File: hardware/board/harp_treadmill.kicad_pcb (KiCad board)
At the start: 4 copper layers, 80 x 100 mm, 133 parts, among them J1 Conn_01x03_Male, J2 AudioJack3, J5 USB_C_Receptacle_USB2.0, J6 Barrel_Jack_Switch, Q1 IRF8707TRPBF, U1 LP2985-3.3, U10 AD8615, U11 INA180A4, U12 UCC27537, U13 LM27762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

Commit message: update sch and pcb
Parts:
- removed R42: 68, Resistor_SMD:R_0402_1005Metric
- removed R44: 49.9, Resistor_SMD:R_0402_1005Metric
- added C34: 100nF, Capacitor_SMD:C_0402_1005Metric, F.Cu at (112.9, 71.0)
- added C35: 100nF, Capacitor_SMD:C_0402_1005Metric, F.Cu at (118.1, 70.0)
- added C36: 100nF, Capacitor_SMD:C_0402_1005Metric, F.Cu at (112.4, 69.2)
- added C61: 1uF, Capacitor_SMD:C_0402_1005Metric, F.Cu at (111.9, 71.0)
- added C62: 10uF, Capacitor_SMD:C_0805_2012Metric, F.Cu at (103.3, 101.5)
- added H1: MountingHole_Pad, kicad_component_library:Terminal_Keystone_779x_EdgeMount_Horizontal, F.Cu at (107.6, 118.4)
- added J3: Conn_01x05_Female, Connector_Phoenix_MC:PhoenixContact_MC_1,5_5-G-3.5_1x05_P3.50mm_Horizontal, F.Cu at (108.1, 41.0)
- added J4: Conn_01x02_Female, Connector_Phoenix_MC:PhoenixContact_MC_1,5_2-G-3.5_1x02_P3.50mm_Horizontal, F.Cu at (108.1, 106.4)
- added J7: Conn_01x04_Female, Connector_Phoenix_MC:PhoenixContact_MC_1,5_4-G-3.5_1x04_P3.50mm_Horizontal, F.Cu at (108.1, 74.8)
- added R14: 10K, Resistor_SMD:R_0402_1005Metric, F.Cu at (111.4, 48.7)
- added R8: 10K, Resistor_SMD:R_0402_1005Metric, F.Cu at (111.4, 43.7)
- moved C41 148.2 mm to (142.4, 122.6), turned to 180 degrees
- moved C46 131.9 mm to (155.2, 94.0), turned to 90 degrees
- moved C49 128.7 mm to (155.2, 92.0), turned to 90 degrees
- moved C42 121.2 mm to (143.1, 116.0), turned to -90 degrees
- moved C43 117.8 mm to (144.4, 116.0), turned to -90 degrees
- moved C48 114.2 mm to (145.7, 116.0), turned to 90 degrees
- moved C8 107.9 mm to (170.5, 51.2), turned to 180 degrees
- moved C60 106.9 mm to (142.3, 46.8), turned to -90 degrees
- moved R31 106.7 mm to (147.2, 113.8), turned to 180 degrees
- moved C44 106.1 mm to (140.0, 44.4)
- moved R32 103.7 mm to (147.2, 114.8)
- moved C40 102.8 mm to (139.9, 42.9), turned to 180 degrees
- moved R22 102.6 mm to (144.4, 84.5), turned to 90 degrees
- moved R23 101.5 mm to (142.9, 84.5), turned to 90 degrees
- moved C39 100.7 mm to (133.1, 115.3)
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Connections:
- U15 pad 2: /Encoder/ENC_A -> /Encoder/ENC_B
- U15 pad 3: /Encoder/ENC_B -> /Encoder/ENC_A
- U4 pad 11: /Harp Core RP2040 + Isolated USB/PIO_POCI0 -> unconnected-(U4-GPIO8-Pad11)
- U4 pad 12: /Harp Core RP2040 + Isolated USB/PIO_SCK0 -> /Harp Core RP2040 + Isolated USB/PIO_CS0
- U4 pad 13: unconnected-(U4-GPIO10-Pad13) -> /Harp Core RP2040 + Isolated USB/PIO_POCI0
- U4 pad 14: /Harp Core RP2040 + Isolated USB/BRAKE_PWM -> /Harp Core RP2040 + Isolated USB/PIO_SCK0
- U4 pad 16: unconnected-(U4-GPIO13-Pad16) -> /Harp Core RP2040 + Isolated USB/BRAKE_PWM
- U4 pad 17: /Encoder/ENC_A -> unconnected-(U4-GPIO14-Pad17)
- U4 pad 18: /Encoder/ENC_B -> unconnected-(U4-GPIO15-Pad18)
- U4 pad 27: unconnected-(U4-GPIO16-Pad27) -> /Encoder/ENC_A
- U4 pad 28: unconnected-(U4-GPIO17-Pad28) -> /Encoder/ENC_B
- U4 pad 9: /Harp Core RP2040 + Isolated USB/PIO_CS0 -> unconnected-(U4-GPIO7-Pad9)
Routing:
- net /Harp Core RP2040 + Isolated USB/HARP_CLK_SYNC: track 6.47 -> 43.6 mm, vias 1 -> 0
- net /Harp Core RP2040 + Isolated USB/BRAKE_PWM: track 0.00 -> 36.2 mm
- net GND: track 31.6 -> 66.9 mm, vias 23 -> 47
- net Net-(U8-~{CS}): track 0.00 -> 33.9 mm
- net /Harp Core RP2040 + Isolated USB/PIO_POCI0: track 0.00 -> 32.9 mm
- net Net-(U8-SCLK): track 0.00 -> 31.3 mm
- net Net-(U9-SCLK): track 0.00 -> 28.5 mm
- net /Harp Core RP2040 + Isolated USB/PIO_POCI1: track 0.00 -> 27.4 mm
- net Net-(U9-~{CS}): track 0.00 -> 26.2 mm
- net Net-(J7-Pin_3): track 0.00 -> 23.6 mm, vias 0 -> 1
- net Net-(J7-Pin_2): track 0.00 -> 23.5 mm, vias 0 -> 1
- net VIN1: track 0.00 -> 17.6 mm, vias 0 -> 5
- net (no net): track 17.3 -> 0.00 mm, vias 6 -> 0
- net GND2: track 0.00 -> 16.7 mm
- net VREF_1V65: track 0.00 -> 15.9 mm, vias 0 -> 3
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- added copper zone on In2.Cu, net +12V
- added copper zone on In2.Cu, net +3V3
- added copper zone on In2.Cu, net +5V
- added copper zone on In2.Cu, net -5V
- added copper zone on In2.Cu, net 5V2
- added copper zone on In2.Cu, net VREF_1V65
- added copper zone on In2.Cu, net VREF_3V3
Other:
- board text added: "5V →"
- board text added: "A →"
- board text added: "B →"
- board text added: "Black →"
- board text added: "DC Power 13-25V"
- board text added: "Fits in: Hammond Manufacturing 1455L801"
- board text added: "GND →"
- board text added: "Green →"
- board text added: "Harp Sync Input ↓"
- board text added: "Red →"
- board text added: "Shield →"
- board text added: "TODO: RFID TODO: OSH Logo"
- board text added: "TODO: Switch 5v2 and 12v"
- board text added: "TODO: remove slot in USBC footprint. TODO: capacitors on 12V source?"
- board text added: "White →"
- board text removed: "Harp Sync Input ↑"
- board text removed: "Power"
- board text removed: "TODO: add a GND LUG?"
- board text removed: "TODO: remove slot in USBC footprint."

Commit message: update schematic; continue pcb draft
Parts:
- removed R14, R8: 10K, Resistor_SMD:R_0402_1005Metric
- added C20: 100pF, Capacitor_SMD:C_0402_1005Metric, F.Cu at (112.5, 44.1)
- added C21: 1000pF, Capacitor_SMD:C_0402_1005Metric, F.Cu at (113.6, 46.2)
- added C22: 100pF, Capacitor_SMD:C_0402_1005Metric, F.Cu at (112.5, 48.3)
- added C23: 100nF, Capacitor_SMD:C_0402_1005Metric, F.Cu at (119.9, 43.2)
- added C25: 100nF, Capacitor_SMD:C_0402_1005Metric, F.Cu at (119.8, 49.2)
- added G***: LOGO, LOGO, B.Cu at (169.5, 100.0)
- added REF**: OSHW-Logo2_7.3x6mm_SilkScreen, Symbol:OSHW-Logo2_7.3x6mm_SilkScreen, B.Cu at (170.6, 126.0)
- added REF**: Symbol_Barrel_Polarity, Symbol:Symbol_Barrel_Polarity, B.Cu at (170.2, 118.0)
- added RN1: 20K, Resistor_SMD:R_Array_Convex_2x0606, F.Cu at (111.8, 46.2)
- R15: footprint Resistor_SMD:R_0603_1608Metric -> Resistor_SMD:R_0603_1608Metric_Pad0.98x0.95mm_HandSolder
- R29: value 1K82 -> 715
- R32: value 715 -> 1K82
- moved R16 12.9 mm to (114.2, 53.4)
- moved C27 12.2 mm to (115.3, 53.4), turned to 90 degrees
- moved R17 12.2 mm to (115.9, 51.9), turned to 180 degrees
- moved C45 6.48 mm to (154.9, 96.4), turned to 0 degrees
- moved C62 5.25 mm to (108.5, 102.2), turned to 180 degrees
- moved R27 5.12 mm to (111.6, 103.6), turned to -90 degrees
- moved C59 4.74 mm to (117.2, 104.3)
- moved U11 4.70 mm to (114.5, 103.7)
- moved C30 4.50 mm to (112.1, 98.9)
- moved U10 4.49 mm to (114.5, 98.9)
- moved TP1 3.99 mm to (127.0, 43.6), turned to 0 degrees
- moved C11 3.34 mm to (152.5, 93.5), turned to -90 degrees
- moved C46 3.29 mm to (156.3, 90.9), turned to 180 degrees
- moved TP2 3.11 mm to (111.4, 94.5), turned to 180 degrees
- moved D5 2.80 mm to (126.5, 45.6)
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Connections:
- C24 pad 1: GND -> +5V
- C24 pad 2: +5V -> GND
- C39 pad 1: 5V2 -> +12V
- C52 pad 1: +12V -> 5V2
- C55 pad 1: +5V -> 5V2
- C57 pad 1: +5V -> 5V2
- C58 pad 2: +5V -> 5V2
- D9 pad 1: Net-(U14-BOOST2) -> Net-(U14-BOOST1)
- D9 pad 2: Net-(U14-BOOST1) -> Net-(U14-BOOST2)
- J7 pad 1: +5V -> 5V2
- L2 pad 1: 5V2 -> +12V
- L3 pad 2: +12V -> 5V2
- R28 pad 2: 5V2 -> +12V
- R29 pad 1: GND -> Net-(U14-FB1)
- R29 pad 2: Net-(U14-FB1) -> GND
- R32 pad 1: Net-(U14-FB2) -> GND
- R32 pad 2: GND -> Net-(U14-FB2)
- R35 pad 1: +12V -> 5V2
- U15 pad 8: +5V -> 5V2
- U4 pad 16: /Harp Core RP2040 + Isolated USB/BRAKE_PWM -> unconnected-(U4-GPIO13-Pad16)
- U4 pad 35: unconnected-(U4-GPIO23-Pad35) -> /Harp Core RP2040 + Isolated USB/BRAKE_PWM
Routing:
- net 5V2: track 6.57 -> 62.1 mm, vias 1 -> 15
- net +3V3: track 43.8 -> 91.5 mm, vias 19 -> 27
- net GND: track 66.9 -> 97.8 mm, vias 47 -> 88
- net -5V: track 1.15 -> 12.2 mm, vias 1 -> 5
- net Net-(D5-K): track 9.06 -> 18.5 mm
- net Net-(D8-K): track 0.00 -> 8.85 mm
- net Net-(D10-K): track 0.00 -> 8.85 mm
- net +12V: track 14.6 -> 22.8 mm, vias 4 -> 8
- net +5V: track 7.44 -> 13.6 mm, vias 1 -> 4
- net Net-(U14-BOOST1): track 0.00 -> 5.96 mm, vias 0 -> 2
- net Net-(U14-BOOST2): track 0.00 -> 5.91 mm, vias 0 -> 2
- net Net-(U10--): track 6.34 -> 10.4 mm
- net Net-(RN1A-R1.2): track 3.13 -> 7.04 mm
- net VREF_1V65: track 15.9 -> 19.7 mm
- net Net-(RN1B-R2.2): track 3.31 -> 7.04 mm
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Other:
- board text added: "+"
- board text added: "-"
- board text added: "DC Power 13-25V, 6W"
- board text added: "Ground"
- board text added: "Oct 31, 2023"
- board text added: "Shield → (if provided)"
- board text added: "Source Files & Setup ↓"
- board text added: "TODO: remove slot in USBC footprint."
- board text removed: "DC Power 13-25V"
- board text removed: "Oct 26, 2023"
- board text removed: "Shield →"
- board text removed: "TODO: RFID TODO: OSH Logo"
- board text removed: "TODO: Switch 5v2 and 12v"
- board text removed: "TODO: remove slot in USBC footprint. TODO: capacitors on 12V source?"

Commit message: wrap up pcb draft
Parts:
- removed D5: D_Zener, Diode_SMD:D_SOD-123F
- added C63: 100nF, Capacitor_SMD:C_0402_1005Metric, F.Cu at (115.7, 53.3)
- added R8: 10K, Resistor_SMD:R_0402_1005Metric, F.Cu at (118.2, 48.9)
- added U16: AD8615, Package_TO_SOT_SMD:TSOT-23-5, F.Cu at (115.6, 51.0)
- moved TP1 20.9 mm to (112.2, 58.3), turned to -90 degrees
- moved C27 3.50 mm to (115.3, 56.9)
- moved C32 3.50 mm to (119.0, 59.6)
- moved R16 3.50 mm to (114.2, 56.9)
- moved R17 3.50 mm to (115.9, 55.4)
- moved R18 3.50 mm to (121.3, 57.1)
- moved U8 3.50 mm to (118.0, 57.4)
- moved G*** 1.20 mm to (169.5, 98.8)
- moved C25 0.10 mm to (119.9, 49.2)
- moved C23 0.10 mm to (120.0, 43.2)
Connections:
- R16 pad 2: Net-(D5-K) -> Net-(U16--)
- TP1 pad 1: Net-(D5-K) -> Net-(U16--)
- U7 pad 7: Net-(D5-K) -> Net-(U7-VOUT)
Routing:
- net Net-(D5-K): track 18.5 -> 0.00 mm
- net Net-(U16--): track 0.00 -> 13.9 mm
- net +3V3: track 91.5 -> 97.7 mm, vias 27 -> 30
- net Net-(U7-VOUT): track 0.00 -> 4.53 mm
- net 5V2: track 62.1 -> 60.0 mm, vias 15 -> 17
- net Net-(U16-+): track 0.00 -> 1.84 mm
- net VREF_1V65: track 19.7 -> 18.1 mm
- net Net-(U8-SCLK): track 31.3 -> 29.8 mm
- net Net-(U8-~{CS}): track 33.7 -> 32.3 mm
- net /Harp Core RP2040 + Isolated USB/PIO_POCI0: track 32.7 -> 31.3 mm
- net /Harp Core RP2040 + Isolated USB/BRAKE_PWM: track 36.1 -> 35.2 mm
- net GND: track 97.8 -> 98.1 mm, vias 88 -> 89
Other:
- board text added: "Harp-compliant rodent treadmill driver board"
- board text added: "{dblquote}Mus Sisyphys{dblquote}"
- board text removed: "Harp Treadmill"
- board text removed: "TODO: remove slot in USBC footprint."

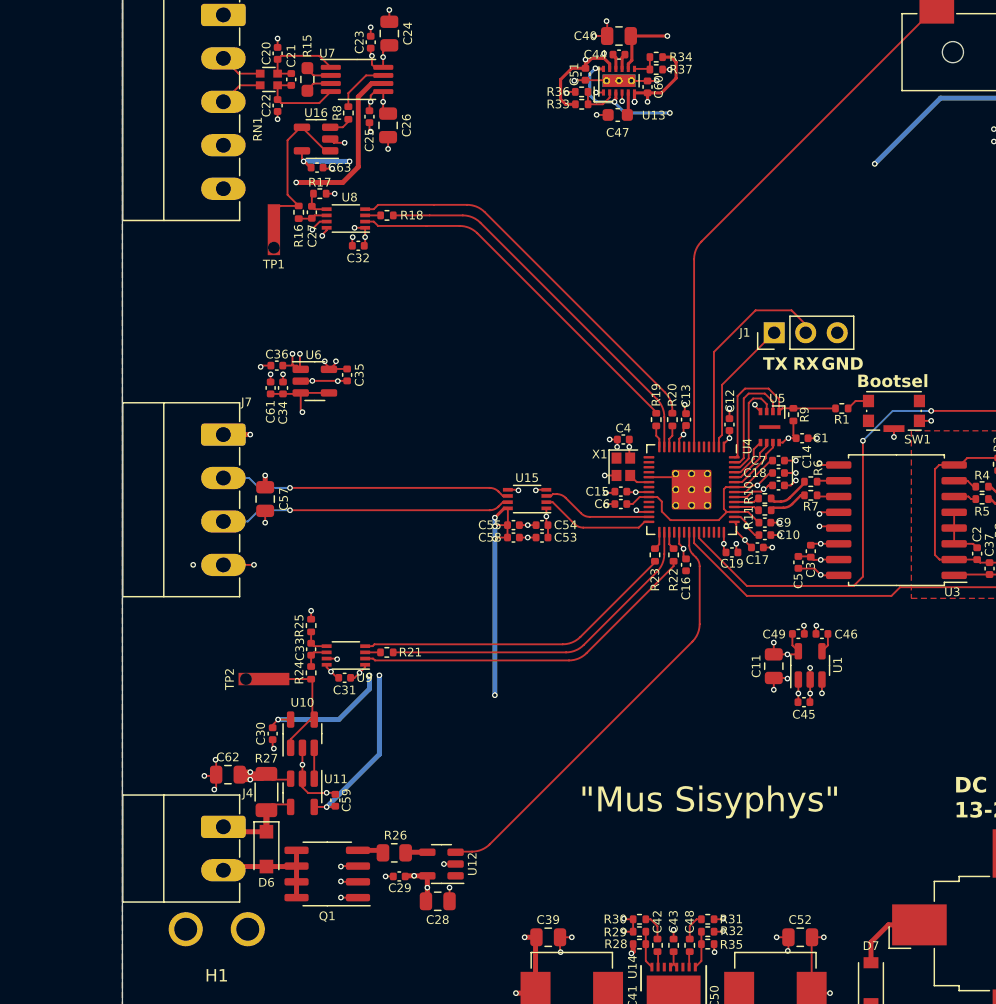
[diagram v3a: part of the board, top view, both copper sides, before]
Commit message: draft layout with analog brake driver circuit
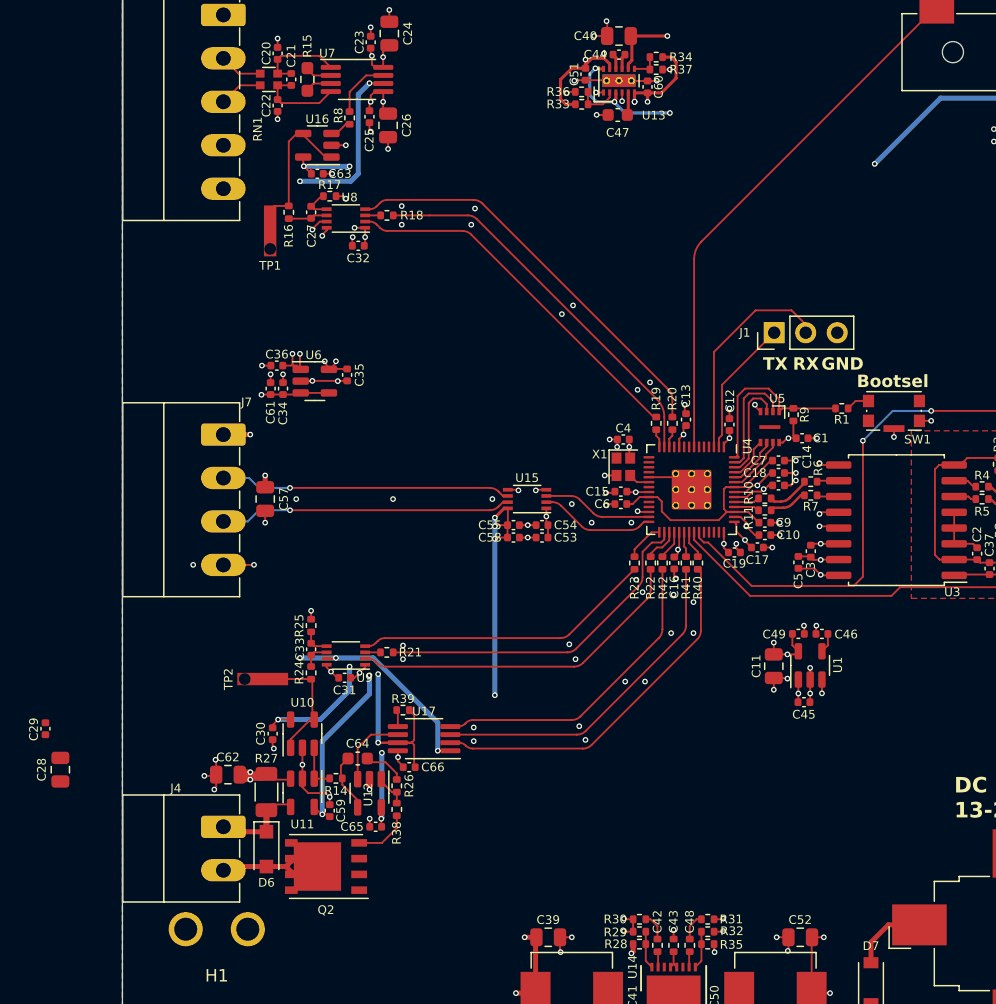
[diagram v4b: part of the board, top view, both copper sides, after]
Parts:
- removed Q1: IRF8707TRPBF, Package_SO:SOIC-8_3.9x4.9mm_P1.27mm
- added C64: 10nF, Capacitor_SMD:C_0603_1608Metric, F.Cu at (119.0, 100.9)
- added C65: 100nF, Capacitor_SMD:C_0402_1005Metric, F.Cu at (120.4, 106.4)
- added C66: 100nF, Capacitor_SMD:C_0402_1005Metric, F.Cu at (123.1, 101.6)
- added Q2: Si7336ADP, Package_SO:PowerPAK_SO-8_Single, F.Cu at (116.4, 109.6)
- added R14: 7K5, Resistor_SMD:R_0402_1005Metric, F.Cu at (117.2, 102.5)
- added R38: 10, Resistor_SMD:R_0402_1005Metric, F.Cu at (122.1, 105.0)
- added R39: 10K, Resistor_SMD:R_0402_1005Metric, F.Cu at (122.6, 97.0)
- added R40: 49.9, Resistor_SMD:R_0402_1005Metric, F.Cu at (146.3, 85.2)
- added R41: 49.9, Resistor_SMD:R_0402_1005Metric, F.Cu at (145.4, 85.2)
- added R42: 49.9, Resistor_SMD:R_0402_1005Metric, F.Cu at (143.5, 85.2)
- added U17: LTC2641, Package_SO:MSOP-8_3x3mm_P0.65mm, F.Cu at (124.3, 99.3)
- R26: value 470 -> 5K1; footprint Resistor_SMD:R_0805_2012Metric -> Resistor_SMD:R_0402_1005Metric
- U12: value UCC27537 -> AD8615; footprint Package_TO_SOT_SMD:SOT-23-5 -> Package_TO_SOT_SMD:TSOT-23-5
- moved C28 32.2 mm to (95.0, 101.8), turned to -90 degrees
- moved C29 30.9 mm to (93.8, 98.5), turned to -90 degrees
- moved U12 8.13 mm to (119.9, 103.7), turned to -90 degrees
- moved R26 5.40 mm to (122.1, 103.1), turned to -90 degrees
- moved R22 1.96 mm to (142.6, 85.2)
- moved R23 1.77 mm to (141.2, 85.2)
- moved C16 0.96 mm to (144.4, 85.2)
- moved C59 0.95 mm to (116.7, 105.1)
- moved R17 0.82 mm to (116.7, 55.6)
- moved R16 0.80 mm to (113.4, 56.9)
- moved U16 0.51 mm to (115.7, 51.5)
- moved C63 0.50 mm to (115.7, 53.8)
- moved R8 0.41 mm to (118.3, 49.3)
- moved TP1 0.32 mm to (111.9, 58.4)
- moved R19 0.30 mm to (143.0, 73.9)
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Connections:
- net /Harp Core RP2040 + Isolated USB/PIO_CS0 renamed /Harp Core RP2040 + Isolated USB/PIO_ADC1_CS
- net /Harp Core RP2040 + Isolated USB/PIO_CS1 renamed /Harp Core RP2040 + Isolated USB/PIO_ADC0_CS
- net /Harp Core RP2040 + Isolated USB/PIO_POCI0 renamed /Harp Core RP2040 + Isolated USB/PIO_ADC1_POCI
- net /Harp Core RP2040 + Isolated USB/PIO_POCI1 renamed /Harp Core RP2040 + Isolated USB/PIO_ADC0_POCI
- net /Harp Core RP2040 + Isolated USB/PIO_SCK0 renamed /Harp Core RP2040 + Isolated USB/PIO_ADC1_SCK
- net /Harp Core RP2040 + Isolated USB/PIO_SCK1 renamed /Harp Core RP2040 + Isolated USB/PIO_ADC0_SCK
- R26 pad 1: Net-(U12-OUT) -> Net-(C64-Pad2)
- R26 pad 2: Net-(Q1-G) -> Net-(R26-Pad2)
- U12 pad 1: unconnected-(U12-EN-Pad1) -> Net-(R26-Pad2)
- U12 pad 3: /Harp Core RP2040 + Isolated USB/BRAKE_PWM -> Net-(U12-+)
- U12 pad 4: Net-(U12-OUT) -> Net-(U12--)
- U12 pad 5: +12V -> 5V2
- U4 pad 32: unconnected-(U4-GPIO21-Pad32) -> /Harp Core RP2040 + Isolated USB/PIO_DAC_PICO
- U4 pad 34: unconnected-(U4-GPIO22-Pad34) -> /Harp Core RP2040 + Isolated USB/PIO_DAC_SCK
- U4 pad 35: /Harp Core RP2040 + Isolated USB/BRAKE_PWM -> /Harp Core RP2040 + Isolated USB/PIO_DAC_CS
- U9 pad 7: VREF_3V3 -> VREF_1V65
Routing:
- net /Harp Core RP2040 + Isolated USB/BRAKE_PWM: track 35.2 -> 0.00 mm
- net Net-(U17-~{CS}): track 0.00 -> 29.4 mm
- net Net-(U17-SCLK): track 0.00 -> 27.3 mm
- net Net-(U17-DIN): track 0.00 -> 25.2 mm
- net VREF_1V65: track 18.1 -> 35.6 mm, vias 3 -> 7
- net +3V3: track 97.7 -> 112.3 mm, vias 30 -> 32
- net Net-(U12-+): track 0.00 -> 6.20 mm
- net 5V2: track 60.0 -> 66.1 mm, vias 17 -> 19
- net Net-(U12--): track 0.00 -> 4.73 mm
- net Net-(Q2-G): track 0.00 -> 4.52 mm
- net +12V: track 22.8 -> 18.9 mm, vias 8 -> 6
- net Net-(C64-Pad2): track 0.00 -> 3.36 mm
- net Net-(D6-A): track 9.84 -> 6.79 mm
- net GND: track 98.1 -> 95.4 mm, vias 89 -> 117
- net Net-(R26-Pad2): track 0.00 -> 2.67 mm
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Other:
- board text removed: "{dblquote}Mus Sisyphys{dblquote}"

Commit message: draft v0.1 pcb
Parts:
- added C67: 100nF, Capacitor_SMD:C_0402_1005Metric, F.Cu at (122.7, 47.1)
- added C68: 100nF, Capacitor_SMD:C_0402_1005Metric, F.Cu at (115.8, 59.5)
- C28: value 10uF -> 100nF; footprint Capacitor_SMD:C_0805_2012Metric -> Capacitor_SMD:C_0402_1005Metric
- moved C28 32.3 mm to (127.3, 101.6), turned to 180 degrees
- moved C29 24.2 mm to (116.7, 90.8), turned to 0 degrees
- moved C8 0.14 mm to (171.5, 51.1)
- moved D4 0.14 mm to (171.5, 50.1)
- moved C65 0.11 mm to (120.5, 106.3)
- moved R16 0.10 mm to (113.3, 56.9)
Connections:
- C28 pad 1: +12V -> GND
- C28 pad 2: GND -> VREF_1V65
- C29 pad 2: +12V -> VREF_1V65
- C48 pad 1: Net-(U14-VC2) -> Net-(U14-PG1)
- U14 pad 10: Net-(U14-VC2) -> Net-(U14-PG1)
- U14 pad 14: unconnected-(U14-PG1-Pad14) -> Net-(U14-PG1)
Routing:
- net GND: track 95.4 -> 121.9 mm, vias 117 -> 135
- net VREF_1V65: track 35.6 -> 45.5 mm
- net Net-(U14-PG1): track 0.00 -> 8.27 mm
- net 5V2: track 66.1 -> 64.8 mm
- net Net-(U14-VC2): track 1.26 -> 0.00 mm
- net VREF_3V3: track 4.63 -> 5.84 mm
- net -5V: track 12.4 -> 12.8 mm, vias 5 -> 4
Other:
- board text added: "Harp Treadmill Driver"
- board text added: "Nov 10, 2023"
- board text added: "V0.1.0"
- board text added: "raw brake sense voltage ↓"
- board text added: "↑ amplified transducer output voltage"
- board text removed: "Oct 31, 2023"
- board text removed: "V0.0.1"

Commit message: update board for v0.2.0
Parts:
- D6: value 1N4007 -> 1N4007FL
- moved C8 4.00 mm to (175.5, 51.1)
- moved D4 4.00 mm to (175.5, 50.1)
- moved J2 3.10 mm to (174.5, 44.0)
- moved TP1 1.43 mm to (111.3, 59.7), turned to 180 degrees
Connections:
- C28 pad 2: VREF_1V65 -> VREF_3V3
- C29 pad 2: VREF_1V65 -> VREF_3V3
- U17 pad 1: VREF_1V65 -> VREF_3V3
- U9 pad 7: VREF_1V65 -> VREF_3V3
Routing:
- net VREF_1V65: track 45.5 -> 20.0 mm, vias 7 -> 4
- net VREF_3V3: track 5.84 -> 25.7 mm, vias 3 -> 5
- net /Harp Core RP2040 + Isolated USB/HARP_CLK_SYNC: track 43.5 -> 46.6 mm
- net +3V3: track 112.6 -> 115.3 mm
- net GND: track 121.9 -> 120.1 mm, vias 135 -> 134
- net Net-(U16--): track 13.0 -> 14.6 mm
